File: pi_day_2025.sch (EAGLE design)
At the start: 105 parts, among them IC1 W25Q64JVXGIQ, J4 SM03B-SRSS-TB(LF)(SN), Q2 310mA/60V/1.6Ω, U1 APS6404L-3SQR-ZR, U2 RP2350A, U3 TPS76318DBVRG4, U4 TPS63001DRCR, U5 TXS0108EPWRG4, U6 LSM6DS3TR-C, U7 MCP73833T-AMI/MF, U8 TPS2113APWR, Y1 12MHz

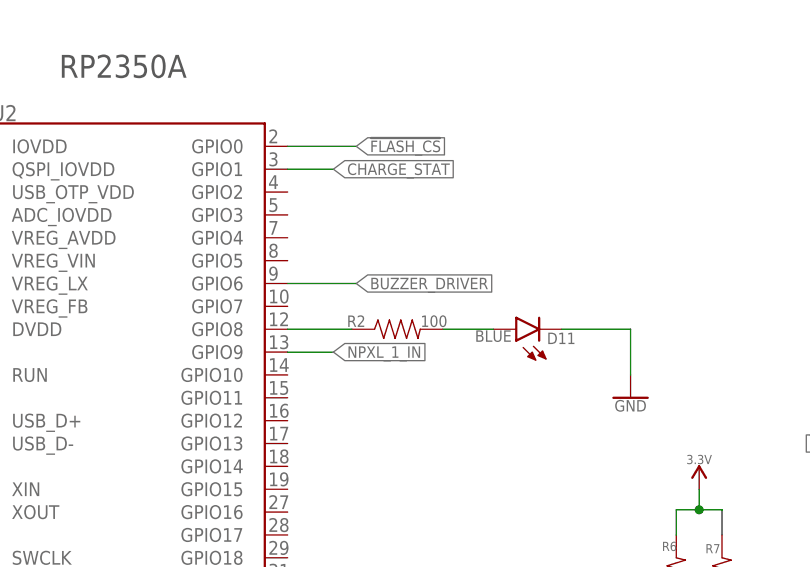
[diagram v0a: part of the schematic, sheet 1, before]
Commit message: Added PDM microphone
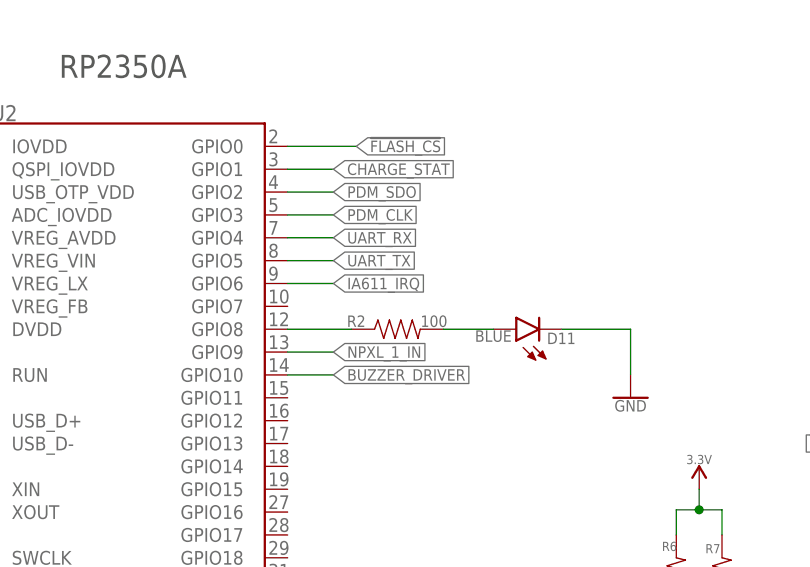
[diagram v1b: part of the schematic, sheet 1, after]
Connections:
- net BUZZER_DRIVER: now also U2.GPIO10; no longer U2.GPIO6
- net IA611_IRQ: now also U2.GPIO6
- net PDM_CLK: now also U2.GPIO3
- net PDM_SDO: now also U2.GPIO2
- net UART_RX: now also U2.GPIO4
- net UART_TX: now also U2.GPIO5
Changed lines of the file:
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@@
-</segment>
-</net>
-<net name="BUZZER_DRIVER" class="0">
-<segment>
-<pinref part="U2" gate="G$1" pin="GPIO6"/>
-<wire x1="119.38" y1="144.78" x2="127" y2="144.78" width="0.1524" layer="91"/>
-<label x="127" y="144.78" size="1.27" layer="95" font="vector" ratio="20" xref="yes"/>
 </segment>
 </net>
@@
 </segment>
 </net>
+<net name="PDM_SDO" class="0">
+<segment>
+<pinref part="U2" gate="G$1" pin="GPIO2"/>
+<wire x1="119.38" y1="154.94" x2="124.46" y2="154.94" width="0.1524" layer="91"/>
+<label x="124.46" y="154.94" size="1.27" layer="95" font="vector" ratio="20" xref="yes"/>
+</segment>
+</net>
+<net name="PDM_CLK" class="0">
+<segment>
+<pinref part="U2" gate="G$1" pin="GPIO3"/>
+<wire x1="119.38" y1="152.4" x2="124.46" y2="152.4" width="0.1524" layer="91"/>
+<label x="124.46" y="152.4" size="1.27" layer="95" font="vector" ratio="20" xref="yes"/>
+</segment>
+</net>
+<net name="UART_RX" class="0">
+<segment>
+<pinref part="U2" gate="G$1" pin="GPIO4"/>
+<wire x1="119.38" y1="149.86" x2="124.46" y2="149.86" width="0.1524" layer="91"/>
+<label x="124.46" y="149.86" size="1.27" layer="95" font="vector" ratio="20" xref="yes"/>
+</segment>
+</net>
+<net name="UART_TX" class="0">
+<segment>
+<pinref part="U2" gate="G$1" pin="GPIO5"/>
+<wire x1="119.38" y1="147.32" x2="124.46" y2="147.32" width="0.1524" layer="91"/>
+<label x="124.46" y="147.32" size="1.27" layer="95" font="vector" ratio="20" xref="yes"/>
+</segment>
+</net>
+<net name="BUZZER_DRIVER" class="0">
+<segment>
+<pinref part="U2" gate="G$1" pin="GPIO10"/>
+<wire x1="119.38" y1="134.62" x2="124.46" y2="134.62" width="0.1524" layer="91"/>
+<label x="124.46" y="134.62" size="1.27" layer="95" font="vector" ratio="20" xref="yes"/>
+</segment>
+</net>
+<net name="IA611_IRQ" class="0">
+<segment>
+<pinref part="U2" gate="G$1" pin="GPIO6"/>
+<wire x1="119.38" y1="144.78" x2="124.46" y2="144.78" width="0.1524" layer="91"/>
+<label x="124.46" y="144.78" size="1.27" layer="95" font="vector" ratio="20" xref="yes"/>
+</segment>
+</net>

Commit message: Added ESP32 chipset.
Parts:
- added C47: 10uF, SparkFun-Capacitors:10UF-0402T-6.3V-20%
- added C48: 0.1uF, SparkFun-Capacitors:0.1UF-0402-6.3V-10%-X7R
- added R23: 10k, SparkFun-Resistors:10KOHM-0402-1/16W-1%
- added U9: ESP32-C3-MINI-1-N4, ESP32-C3-MINI-1-N4:ESP32-C3-MINI-1-N4
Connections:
- new net !ESP32_BOOT: U2.GPIO19, U9.IO9
- new net !ESP32_RST: U2.GPIO18, U9.EN
- new net ESP32_CS: U2.GPIO21, U9.IO10
- new net ESP32_HANDSHAKE: U2.GPIO17, U9.IO3
- new net ESP32_MISO: U2.GPIO20, U9.IO2
- new net ESP32_MOSI: U2.GPIO23, U9.IO7
- new net ESP32_RX: U2.GPIO12, U9.RXD0
- new net ESP32_SCK: U2.GPIO22, U9.IO6
- new net ESP32_TX: U2.GPIO13, U9.TXD0
- new net N$25: R23.1, U9.IO8
- net 3.3V: now also C47.1, C48.1, R23.2, U9.3V3
- net GND: now also C47.2, C48.2, U9.GND
- net LSM6_INT1: now also U2.GPIO15
- net LSM6_INT2: now also U2.GPIO16
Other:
- note added: "ESP32 Co-Processor"

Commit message: COmpleted schematic
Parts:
- CONN1: value GT-USB_8012A -> TYPE-C-31-M-12; device GT_USB-8012A:GT-USB_8012A -> TYPE-C-31-M-12:TYPE-C-31-M-12
- R14: value (none) -> 499
- R3, R8: value (none) -> 5.1K
- R4: value (none) -> DNF
- R5: value (none) -> 1K
- R6, R7: value (none) -> 2.2K
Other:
- moved on the sheet: CONN1
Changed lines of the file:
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@@
 <part name="GND8" library="SparkFun-PowerSymbols" library_urn="urn:adsk.eagle:library:530" deviceset="GND" device=""/>
 <part name="FRAME2" library="SparkFun-Aesthetics" library_urn="urn:adsk.eagle:library:507" deviceset="FRAME-A4L" device=""/>
-<part name="R3" library="SparkFun-Resistors" library_urn="urn:adsk.eagle:library:532" deviceset="RESISTOR" device="0402" package3d_urn="urn:adsk.eagle:package:39657@1/2" override_package3d_urn="urn:adsk.eagle:package:44163397/2" override_package_urn="urn:adsk.eagle:footprint:39625/1" override_locally_modified="yes" value=" "/>
+<part name="R3" library="SparkFun-Resistors" library_urn="urn:adsk.eagle:library:532" deviceset="RESISTOR" device="0402" package3d_urn="urn:adsk.eagle:package:39657@1/2" override_package3d_urn="urn:adsk.eagle:package:44163397/2" override_package_urn="urn:adsk.eagle:footprint:39625/1" override_locally_modified="yes" value="5.1K"/>
 <part name="GND6" library="SparkFun-PowerSymbols" library_urn="urn:adsk.eagle:library:530" deviceset="GND" device=""/>
 <part name="L1" library="LQW18AN2N2D10D" deviceset="LQW18AN2N2D10D" device="" override_package3d_urn="urn:adsk.eagle:package:44163399/2" override_package_urn="urn:adsk.eagle:footprint:37563/1" override_locally_modified="yes" value="2.2nH"/>
@@
 <part name="C17" library="SparkFun-Capacitors" library_urn="urn:adsk.eagle:library:510" deviceset="0.1UF" device="-0402-16V-10%" package3d_urn="urn:adsk.eagle:package:41385089/1" override_package3d_urn="urn:adsk.eagle:package:46455631/2" override_package_urn="urn:adsk.eagle:footprint:41385037/1" value="0.1uF"/>
 <part name="GND15" library="SparkFun-PowerSymbols" library_urn="urn:adsk.eagle:library:530" deviceset="GND" device=""/>
-<part name="R4" library="SparkFun-Resistors" library_urn="urn:adsk.eagle:library:532" deviceset="RESISTOR" device="0402" package3d_urn="urn:adsk.eagle:package:39657@1/2" override_package3d_urn="urn:adsk.eagle:package:44163374/2" override_package_urn="urn:adsk.eagle:footprint:39625/1" override_locally_modified="yes" value=" "/>
-<part name="R5" library="SparkFun-Resistors" library_urn="urn:adsk.eagle:library:532" deviceset="RESISTOR" device="0402" package3d_urn="urn:adsk.eagle:package:39657@1/2" override_package3d_urn="urn:adsk.eagle:package:44163373/2" override_package_urn="urn:adsk.eagle:footprint:39625/1" override_locally_modified="yes" value=" "/>
-<part name="R6" library="SparkFun-Resistors" library_urn="urn:adsk.eagle:library:532" deviceset="RESISTOR" device="0402" package3d_urn="urn:adsk.eagle:package:39657@1/2" override_package3d_urn="urn:adsk.eagle:package:44163371/3" override_package_urn="urn:adsk.eagle:footprint:39625/1" override_locally_modified="yes" value=" "/>
-<part name="R7" library="SparkFun-Resistors" library_urn="urn:adsk.eagle:library:532" deviceset="RESISTOR" device="0402" package3d_urn="urn:adsk.eagle:package:39657@1/2" override_package3d_urn="urn:adsk.eagle:package:44163370/2" override_package_urn="urn:adsk.eagle:footprint:39625/1" override_locally_modified="yes" value=" "/>
+<part name="R4" library="SparkFun-Resistors" library_urn="urn:adsk.eagle:library:532" deviceset="RESISTOR" device="0402" package3d_urn="urn:adsk.eagle:package:39657@1/2" override_package3d_urn="urn:adsk.eagle:package:44163374/2" override_package_urn="urn:adsk.eagle:footprint:39625/1" override_locally_modified="yes" value="DNF"/>
+<part name="R5" library="SparkFun-Resistors" library_urn="urn:adsk.eagle:library:532" deviceset="RESISTOR" device="0402" package3d_urn="urn:adsk.eagle:package:39657@1/2" override_package3d_urn="urn:adsk.eagle:package:44163373/2" override_package_urn="urn:adsk.eagle:footprint:39625/1" override_locally_modified="yes" value="1K"/>
+<part name="R6" library="SparkFun-Resistors" library_urn="urn:adsk.eagle:library:532" deviceset="RESISTOR" device="0402" package3d_urn="urn:adsk.eagle:package:39657@1/2" override_package3d_urn="urn:adsk.eagle:package:44163371/3" override_package_urn="urn:adsk.eagle:footprint:39625/1" override_locally_modified="yes" value="2.2K"/>
+<part name="R7" library="SparkFun-Resistors" library_urn="urn:adsk.eagle:library:532" deviceset="RESISTOR" device="0402" package3d_urn="urn:adsk.eagle:package:39657@1/2" override_package3d_urn="urn:adsk.eagle:package:44163370/2" override_package_urn="urn:adsk.eagle:footprint:39625/1" override_locally_modified="yes" value="2.2K"/>
 <part name="SUPPLY10" library="SparkFun-PowerSymbols" library_urn="urn:adsk.eagle:library:530" deviceset="3.3V" device=""/>
-<part name="CONN1" library="GT_USB-8012A" deviceset="GT-USB_8012A" device="" override_package3d_urn="urn:adsk.eagle:package:44161671/9" override_package_urn="urn:adsk.eagle:footprint:44161672/1"/>
+<part name="CONN1" library="TYPE-C-31-M-12" deviceset="TYPE-C-31-M-12" device="" override_package3d_urn="urn:adsk.eagle:package:44161671/9" override_package_urn="urn:adsk.eagle:footprint:44161672/1" override_locally_modified="yes"/>
 <part name="GND20" library="SparkFun-PowerSymbols" library_urn="urn:adsk.eagle:library:530" deviceset="GND" device=""/>
-<part name="R8" library="SparkFun-Resistors" library_urn="urn:adsk.eagle:library:532" deviceset="RESISTOR" device="0402" package3d_urn="urn:adsk.eagle:package:39657@1/2" override_package3d_urn="urn:adsk.eagle:package:44163391/2" override_package_urn="urn:adsk.eagle:footprint:39625/1" override_locally_modified="yes" value=" "/>
+<part name="R8" library="SparkFun-Resistors" library_urn="urn:adsk.eagle:library:532" deviceset="RESISTOR" device="0402" package3d_urn="urn:adsk.eagle:package:39657@1/2" override_package3d_urn="urn:adsk.eagle:package:44163391/2" override_package_urn="urn:adsk.eagle:footprint:39625/1" override_locally_modified="yes" value="5.1K"/>
 <part name="GND24" library="SparkFun-PowerSymbols" library_urn="urn:adsk.eagle:library:530" deviceset="GND" device=""/>
 <part name="U2" library="RP2350A" deviceset="RP2350A" device="" override_package3d_urn="urn:adsk.eagle:package:46113661/2" override_package_urn="urn:adsk.eagle:footprint:46113662/1"/>
@@
 <part name="R10" library="SparkFun-Resistors" library_urn="urn:adsk.eagle:library:532" deviceset="100KOHM" device="-0402-1/16W-1%" package3d_urn="urn:adsk.eagle:package:39657@1/2" value="100K"/>
 <part name="GND23" library="SparkFun-PowerSymbols" library_urn="urn:adsk.eagle:library:530" deviceset="GND" device=""/>
-<part name="R14" library="SparkFun-Resistors" library_urn="urn:adsk.eagle:library:532" deviceset="RESISTOR" device="0402" package3d_urn="urn:adsk.eagle:package:39657@1/2" value=" "/>
+<part name="R14" library="SparkFun-Resistors" library_urn="urn:adsk.eagle:library:532" deviceset="RESISTOR" device="0402" package3d_urn="urn:adsk.eagle:package:39657@1/2" value="499"/>
 <part name="SUPPLY19" library="SparkFun-PowerSymbols" library_urn="urn:adsk.eagle:library:530" deviceset="V_USB" device=""/>
 <part name="C14" library="SparkFun-Capacitors" library_urn="urn:adsk.eagle:library:510" deviceset="0.1UF" device="-0402-10V-10%-X7R" package3d_urn="urn:adsk.eagle:package:41385089/1" value="0.1uF"/>

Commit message: Finished schematic
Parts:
- removed C1: 0.1uF, SparkFun-Capacitors:0.1UF-0402T-16V-10%-X7R-WE
- removed C10, C11, C8, C9: 0.1uF, SparkFun-Capacitors:0.1UF-0402-10V-10%-X7R
- removed C47: 10uF, SparkFun-Capacitors:10UF-0402T-6.3V-20%
- removed C48: 0.1uF, SparkFun-Capacitors:0.1UF-0402-6.3V-10%-X7R
- removed D10, D7, D8, D9: SK6812-EJ, SK6812-E:SK6812-EJ
- removed R1, R23: 10k, SparkFun-Resistors:10KOHM-0402-1/16W-1%
- removed U1: APS6404L-3SQR-ZR, RP2350A:APS6404L-3SQR-ZR
- removed U9: ESP32-C3-MINI-1-N4, ESP32-C3-MINI-1-N4:ESP32-C3-MINI-1-N4
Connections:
- removed net !ESP32_BOOT: U2.GPIO19, U9.IO9
- removed net !ESP32_RST: U2.GPIO18, U9.EN
- removed net !FLASH_CS: R1.2, U1.!CE!, U2.GPIO0
- removed net ESP32_CS: U2.GPIO21, U9.IO10
- removed net ESP32_HANDSHAKE: U2.GPIO17, U9.IO3
- removed net ESP32_MISO: U2.GPIO20, U9.IO2
- removed net ESP32_MOSI: U2.GPIO23, U9.IO7
- removed net ESP32_RX: U2.GPIO12, U9.RXD0
- removed net ESP32_SCK: U2.GPIO22, U9.IO6
- removed net ESP32_TX: U2.GPIO13, U9.TXD0
- removed net N$25: R23.1, U9.IO8
- removed net NPXL_6_OUT: D6.DOUT, D7.DIN
- removed net NPXL_7_OUT: D7.DOUT, D8.DIN
- removed net NPXL_8_OUT: D8.DOUT, D9.DIN
- removed net NPXL_9_OUT: D10.DIN, D9.DOUT
- net 3.3V: no longer C1.1, C10.1, C11.1, C47.1, C48.1, C8.1, C9.1, D10.VDD, D7.VDD, D8.VDD, D9.VDD, R1.1, R23.2, U1.VDD, U9.3V3
- net GND: no longer C1.2, C10.2, C11.2, C47.2, C48.2, C8.2, C9.2, D10.GND, D7.GND, D8.GND, D9.GND, U1.VSS, U9.GND
- net QSPI_CLK: no longer U1.SCLK
- net SIO0: no longer U1.SI/SIO0
- net SIO1: no longer U1.SO/SIO1
- net SIO2: no longer U1.SIO2
- net SIO3: no longer U1.SIO3
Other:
- note removed: "ESP32 Co-Processor"
- note removed: "PSRAM"
